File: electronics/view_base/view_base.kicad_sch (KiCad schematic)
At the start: 106 parts, among them J1 BLDC, J2 USB_C_Receptacle_USB2.0, J3 LCD, J4 A, J5 B, Q1 MMBT4403, Q2 UMH3N, U1 MT6701-CT, U2 T-Micro32_Plus, U3 CH340C, U4 HX711, U5 TMC6300, U6 AP2114HA-3.3, U7 SN74LV1T34DBV, U8 VEML7700

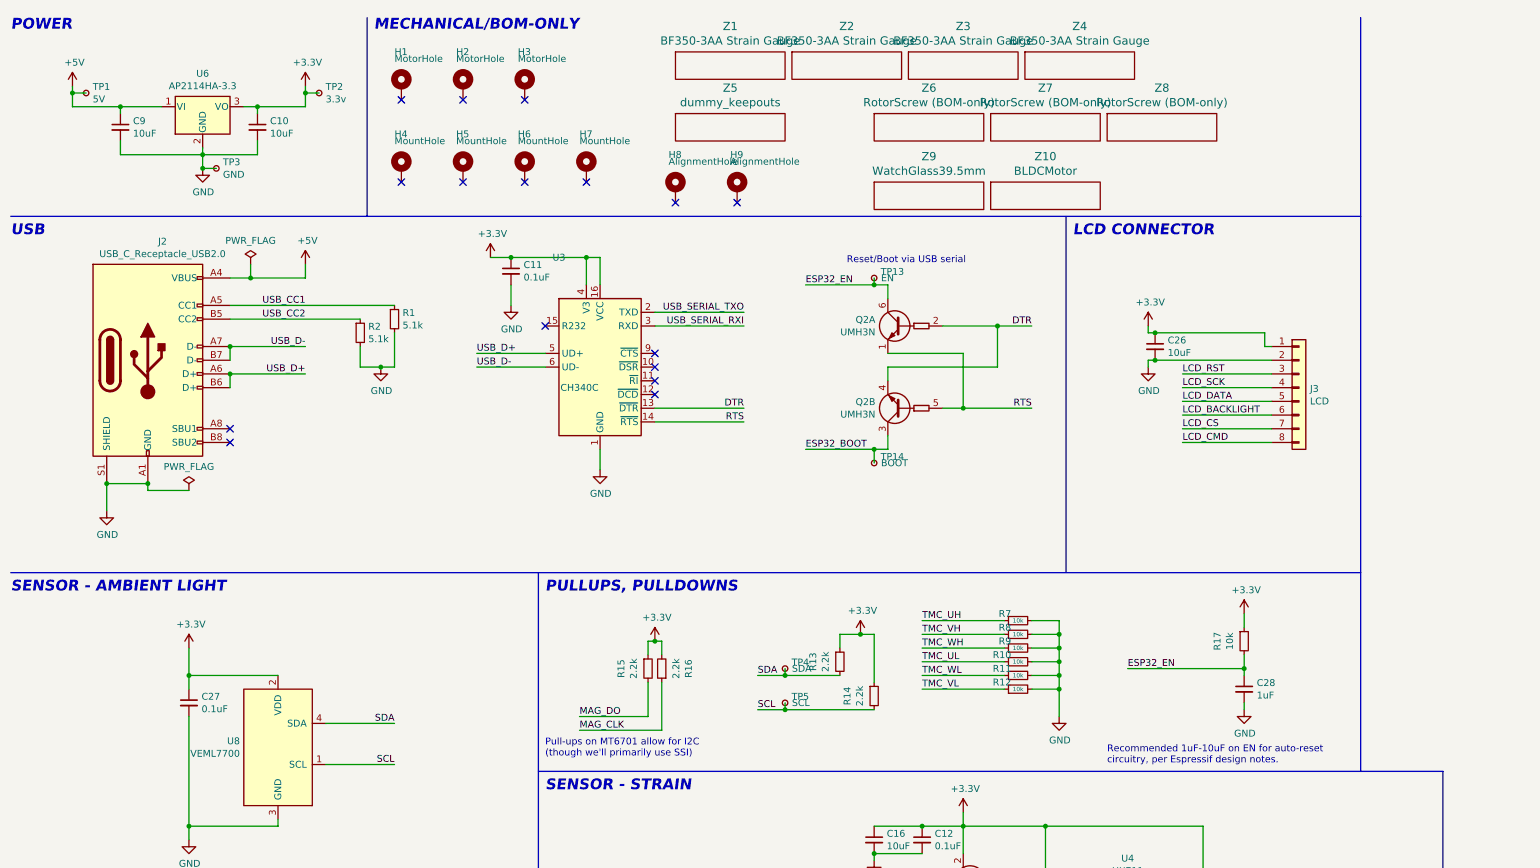
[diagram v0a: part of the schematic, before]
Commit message: Adding second footprint for 3V3 voltage regulator (#98)
The voltage regulator that was originally used isn't available at the moment. To provide more options, a second footprint was added to the PCB for an alternative regulator that has a different pinout. Important to note that only one regulator should be used.

Also, adjusted .gitignore for Mac files and KiCad auto-generated backups.
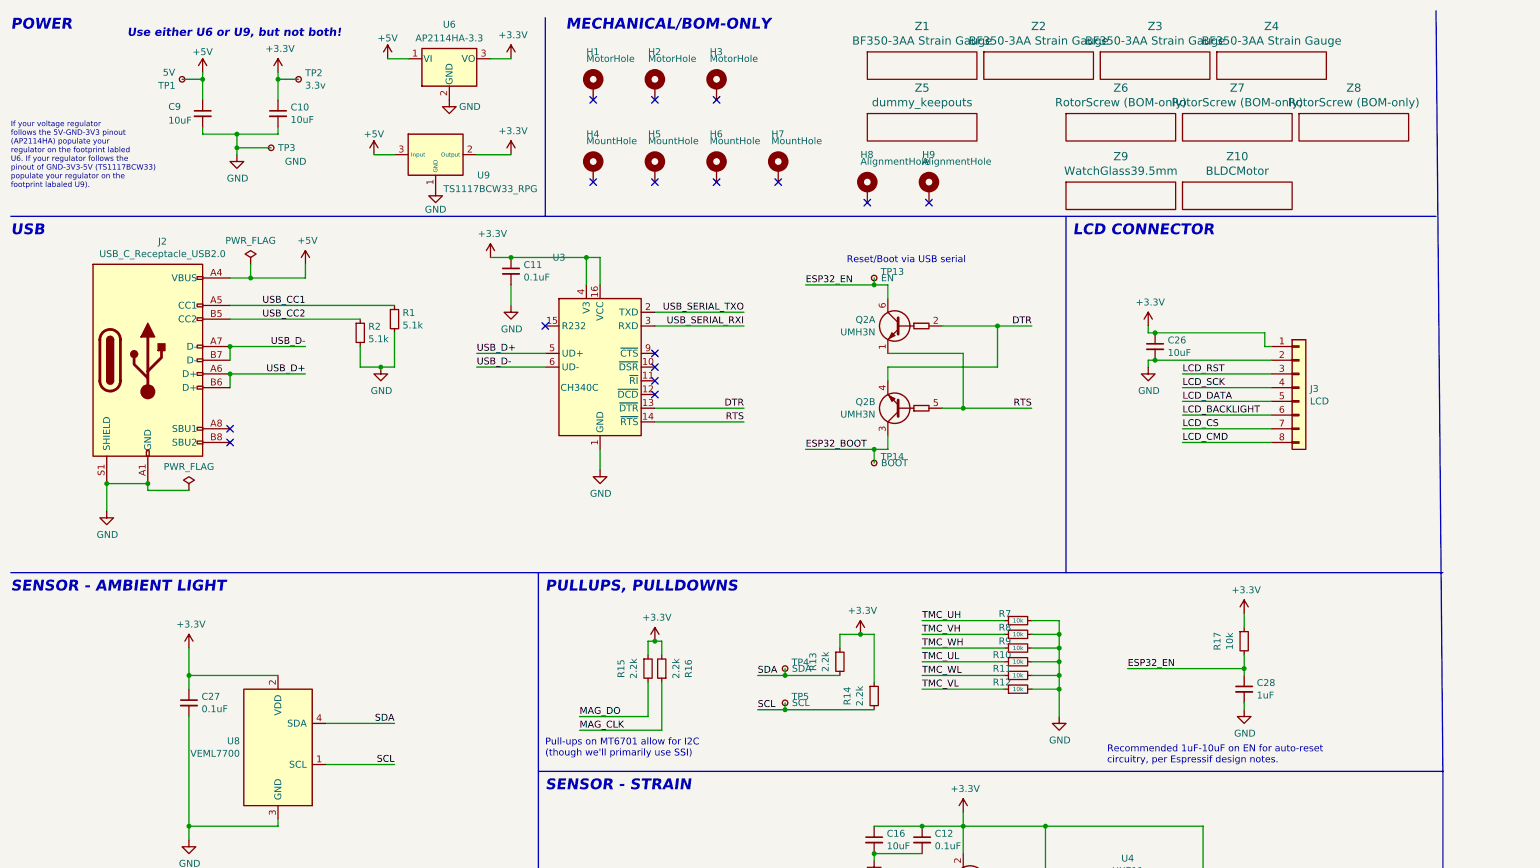
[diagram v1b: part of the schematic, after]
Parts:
- added U9: TS1117BCW33_RPG, Package_TO_SOT_SMD:SOT-223-3_TabPin2, symbol Regulator_Linear:TS1117BCW33_RPG
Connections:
- net +3V3: now also U9.2 (Output)
- net +5V: now also U9.3 (Input)
- net GND: now also U9.1 (GND)
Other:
- note added: "If your voltage regulator follows the 5V-GND-3V3 pinout (AP2114HA) populate your regulator on the footprint labled U6. If your regulator follows the pinout of GND-3V3-5V (TS1117BCW33) populate your regulator on the footprint labaled U9)."
- note added: "Use either U6 or U9, but not both!"
- moved on the sheet: C10, C9, H1, H2, H3, H4, H5, H6, H7, H8, H9, TP1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

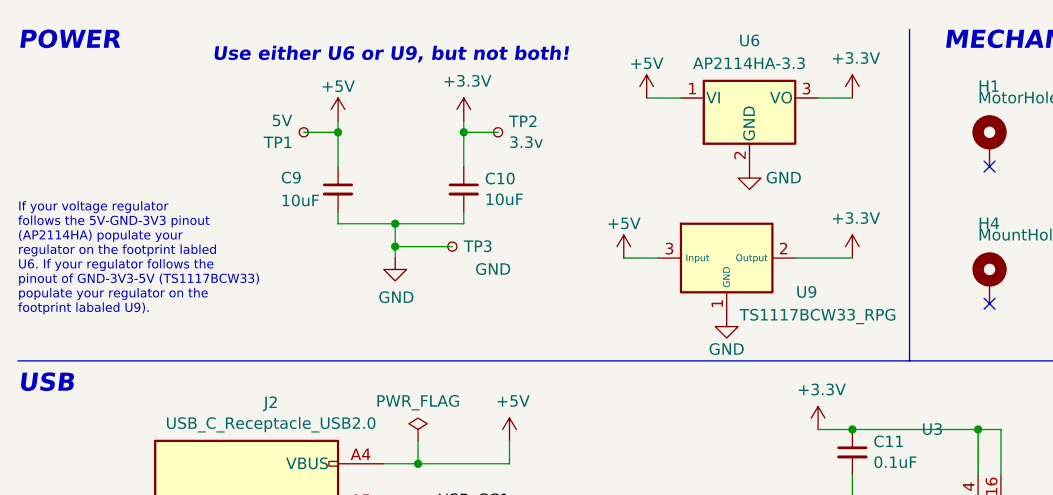
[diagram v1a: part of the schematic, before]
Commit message: Add BOM entries and note for new LDO
Also clean up PCB:
- Make LDOs mirror each other on board
- Custom footprints with silkscreen "in" "gnd" "out" labels
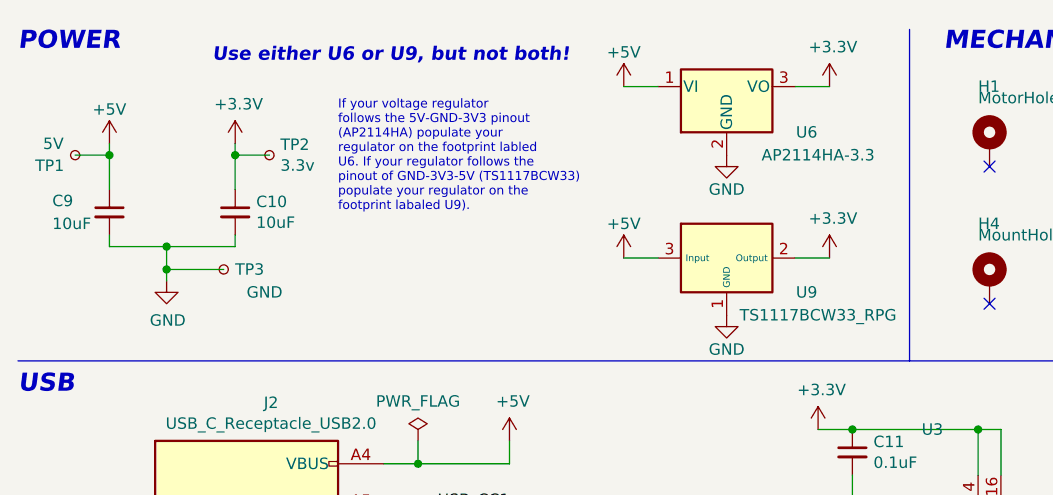
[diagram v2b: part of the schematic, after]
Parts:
- NT1: now left out of the parts list
- U6: Digikey AP2114HA-3.3TRG1DICT-ND -> AP2114HA-3.3TRG1DICT-ND, or MIC39100-3.3WS-CT-ND; Note (none) -> Populate either U6 or U9 - depending on pinout - but not bo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
- U9: Digikey (none) -> 296-35976-1-ND; LCSC (none) -> C6186, C35879, or others; Mouser (none) -> 821-TS1117BCW33RPG; Note (none) -> Populate either U6 or U9 - depending on pinout - but not bo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
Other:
- moved on the sheet: C10, C9, TP1, TP2, TP3, U6

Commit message: Add alternative MT6701 LCSC/JLC part number
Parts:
- U1: LCSC C2856764 -> C2856764, or C3003196
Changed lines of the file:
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@@
       (effects (font (size 1.27 1.27)) hide)
     )
-    (property "LCSC" "C2856764" (id 4) (at 58.42 195.58 0)
+    (property "LCSC" "C2856764, or C3003196" (id 4) (at 58.42 195.58 0)
       (effects (font (size 1.27 1.27)) hide)
     )

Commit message: LCSC part numbers and notes for M1.6/M2 hardware
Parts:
- H1, H2, H3: LCSC (none) -> C2931389; Note Screw: M1.6x10 (countersunk), or M1.6x9 (pan/round) -> Screw: M1.6x10 (countersunk), or M1.6x9 (pan/round). LCSC m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
- H4, H5, H6, H7: LCSC (none) -> C2911210 or C2911532 (screw), C2961595 (nut); Note Screw: M2x5 (pan/round); Nut: M2 hex -> Screw: M2x5 (pan/round); Nut: M2 hex. LCSC min qty 50 (but 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
- Z6, Z7, Z8: Note Screw: M1.6x3 (countersunk) -> Screw: M1.6x3 (countersunk). LCSC C2931384 could work, but 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
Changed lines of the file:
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@@
       (effects (font (size 1.27 1.27)) hide)
     )
-    (property "Note" "Screw: M1.6x10 (countersunk), or M1.6x9 (pan/round)" (id 4) (at 120.65 25.4 0)
+    (property "Note" "Screw: M1.6x10 (countersunk), or M1.6x9 (pan/round). LCSC min qty 50 (but still very cheap)" (id 4) (at 120.65 25.4 0)
+      (effects (font (size 1.27 1.27)) hide)
+    )
+    (property "LCSC" "C2931389" (id 5) (at 120.65 25.4 0)
       (effects (font (size 1.27 1.27)) hide)
     )
@@
       (effects (font (size 1.27 1.27)) hide)
     )
-    (property "Note" "Screw: M1.6x10 (countersunk), or M1.6x9 (pan/round)" (id 4) (at 132.08 25.4 0)
+    (property "Note" "Screw: M1.6x10 (countersunk), or M1.6x9 (pan/round). LCSC min qty 50 (but still very cheap)" (id 4) (at 132.08 25.4 0)
+      (effects (font (size 1.27 1.27)) hide)
+    )
+    (property "LCSC" "C2931389" (id 5) (at 132.08 25.4 0)
       (effects (font (size 1.27 1.27)) hide)
     )
@@
       (effects (font (size 1.27 1.27)) hide)
     )
-    (property "Note" "Screw: M1.6x10 (countersunk), or M1.6x9 (pan/round)" (id 4) (at 143.51 25.4 0)
+    (property "Note" "Screw: M1.6x10 (countersunk), or M1.6x9 (pan/round). LCSC min qty 50 (but still very cheap)" (id 4) (at 143.51 25.4 0)
+      (effects (font (size 1.27 1.27)) hide)
+    )
+    (property "LCSC" "C2931389" (id 5) (at 143.51 25.4 0)
       (effects (font (size 1.27 1.27)) hide)
     )
@@
       (effects (font (size 1.27 1.27)) hide)
     )
-    (property "Note" "Screw: M2x5 (pan/round); Nut: M2 hex" (id 4) (at 120.65 40.64 0)
+    (property "Note" "Screw: M2x5 (pan/round); Nut: M2 hex. LCSC min qty 50 (but still very cheap)" (id 4) (at 120.65 40.64 0)
+      (effects (font (size 1.27 1.27)) hide)
+    )
+    (property "LCSC" "C2911210 or C2911532 (screw), C2961595 (nut)" (id 5) (at 120.65 40.64 0)
       (effects (font (size 1.27 1.27)) hide)
     )
@@
       (effects (font (size 1.27 1.27)) hide)
     )
-    (property "Note" "Screw: M2x5 (pan/round); Nut: M2 hex" (id 4) (at 132.08 40.64 0)
+    (property "Note" "Screw: M2x5 (pan/round); Nut: M2 hex. LCSC min qty 50 (but still very cheap)" (id 4) (at 132.08 40.64 0)
+      (effects (font (size 1.27 1.27)) hide)
+    )
+    (property "LCSC" "C2911210 or C2911532 (screw), C2961595 (nut)" (id 5) (at 132.08 40.64 0)
       (effects (font (size 1.27 1.27)) hide)
     )
@@
       (effects (font (size 1.27 1.27)) hide)
     )
-    (property "Note" "Screw: M2x5 (pan/round); Nut: M2 hex" (id 4) (at 143.51 40.64 0)
+    (property "Note" "Screw: M2x5 (pan/round); Nut: M2 hex. LCSC min qty 50 (but still very cheap)" (id 4) (at 143.51 40.64 0)
+      (effects (font (size 1.27 1.27)) hide)
+    )
+    (property "LCSC" "C2911210 or C2911532 (screw), C2961595 (nut)" (id 5) (at 143.51 40.64 0)
       (effects (font (size 1.27 1.27)) hide)
     )
@@
       (effects (font (size 1.27 1.27)) hide)
     )
-    (property "Note" "Screw: M2x5 (pan/round); Nut: M2 hex" (id 4) (at 154.94 40.64 0)
+    (property "Note" "Screw: M2x5 (pan/round); Nut: M2 hex. LCSC min qty 50 (but still very cheap)" (id 4) (at 154.94 40.64 0)
+      (effects (font (size 1.27 1.27)) hide)
+    )
+    (property "LCSC" "C2911210 or C2911532 (screw), C2961595 (nut)" (id 5) (at 154.94 40.64 0)
       (effects (font (size 1.27 1.27)) hide)
     )
@@
       (effects (font (size 1.524 1.524)) hide)
     )
-    (property "Note" "Screw: M1.6x3 (countersunk)" (id 4) (at 218.44 33.02 0)
+    (property "Note" "Screw: M1.6x3 (countersunk). LCSC C2931384 could work, but tall hex socket head leaves very little clearance for soldered screen PCB wires. Beware: long screws may scrape internal motor stator windings!" (id 4) (at 218.44 33.02 0)
       (effects (font (size 1.27 1.27)) hide)
     )
@@
       (effects (font (size 1.524 1.524)) hide)
     )
-    (property "Note" "Screw: M1.6x3 (countersunk)" (id 4) (at 240.03 33.02 0)
+    (property "Note" "Screw: M1.6x3 (countersunk). LCSC C2931384 could work, but tall hex socket head leaves very little clearance for soldered screen PCB wires. Beware: long screws may scrape internal motor stator windings!" (id 4) (at 240.03 33.02 0)
       (effects (font (size 1.27 1.27)) hide)
     )
@@
       (effects (font (size 1.524 1.524)) hide)
     )
-    (property "Note" "Screw: M1.6x3 (countersunk)" (id 4) (at 261.62 33.02 0)
-      (effects (font (size 1.27 1.27)) hide)
-    )
+    (property "Note" "Screw: M1.6x3 (countersunk). LCSC C2931384 could work, but tall hex socket head leaves very little clearance for soldered screen PCB wires. Beware: long screws may scrape internal motor stator windings!" (id 4) (at 261.62 33.02 0)
+      (effects (font (size 1.27 1.27)) hide)
+    )
